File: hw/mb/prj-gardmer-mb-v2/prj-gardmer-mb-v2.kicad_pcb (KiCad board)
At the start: 2 copper layers, 147 x 71 mm, 176 parts, among them J1 Conn_01x05, J2 230VAC_IN, J3 Conn_01x04, J4 5VDC_IN, K1 AZ9371T-1A-5D, K2 AZ9371T-1A-5D, K3 AZ9371T-1A-5D, K4 AZ9371T-1A-5D, Q1 BC817, Q13 BC817, Q14 BC817, Q2 BC817, Q3 BC817, Q4 BC817, Q5 BC807, Q6 BC807, Q7 BC807, Q8 BC807, Q9 BC817, SW1 Reset_SW, SW10 Unlock_SW, SW2 Clear_SW, SW3 Minutes_SW, SW4 Hours_SW, SW5 Mode_SW, SW6 Relay1_SW, SW7 Relay2_SW, SW8 Relay3_SW, SW9 Relay4_SW, U1 PIC18F25Q10, U2 PCF8523T, U3 74LS166, U4 74HC595, U5 74HC595, U6 ULN2803A, U7 KW4-804AVB, U8 74HC595, Y1 8MHz, Y2 32.768kHz

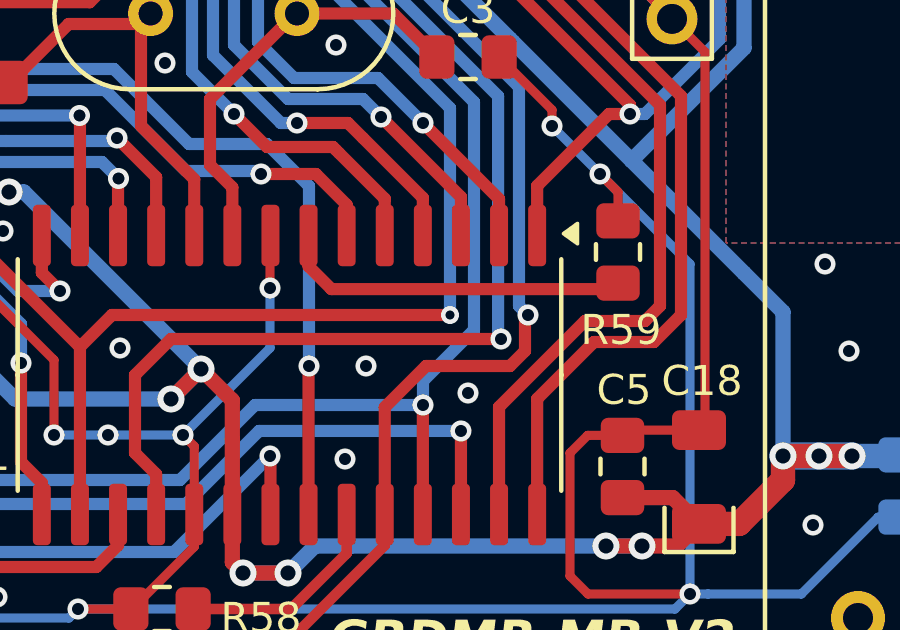
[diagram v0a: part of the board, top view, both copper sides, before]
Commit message: Updated PCB: - set soldermask expansion to 0.1mm (making the pads unmasked by 0.1mm more than their size)
Created production (gerber) files.
Created the release (rev001) of prj-gardmer-mb-v2 hardware.
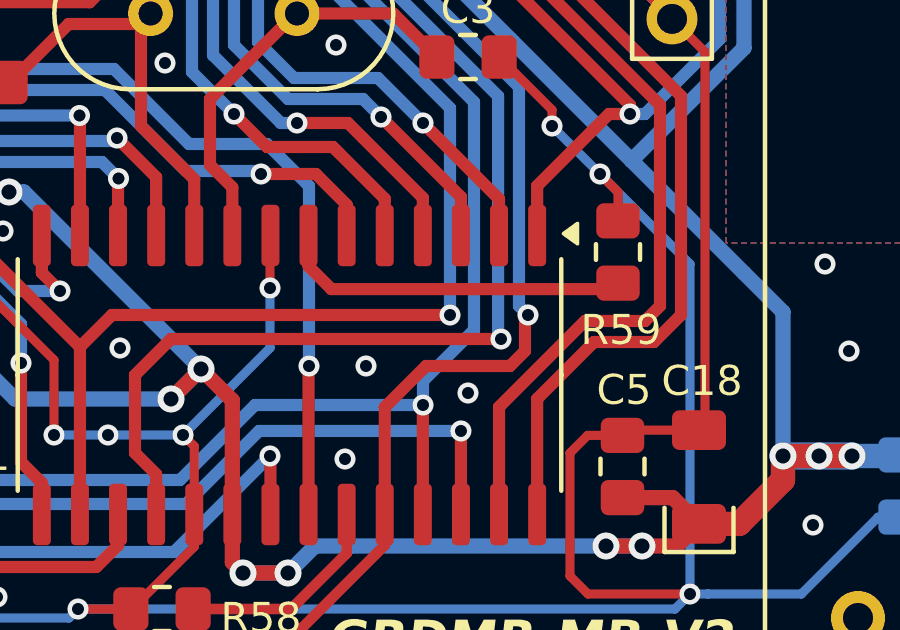
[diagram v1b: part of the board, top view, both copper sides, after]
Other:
- rule pad_to_mask_clearance: 0 -> 0.1

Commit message: Updated the hw release of prj-gardmer-mb-v2 rev001: - reorganized files in catalogues - added schematic in .pdf - added top & bottom elements on pcb in .pdf - added bom
Updated schematic:
- added a title, rev and date to the drawing info table on each sheet
- excluded test points ('TP' elements) from BOM

Updated PCB:
- added a title, rev and date to the drawing info table
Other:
- board text added: "001"
- board text added: "15.05.2025"
- board text added: "prj-gardmer-mb-v2"
